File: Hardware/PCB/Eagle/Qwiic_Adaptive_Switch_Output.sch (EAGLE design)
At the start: 60 parts, among them J1 QWIIC_RIGHT_ANGLE, J3 QWIIC_RIGHT_ANGLE, K1 G3VM-41DY1, K2 G3VM-41DY1, SW1 CUI_SJ1-3513, SW2 CUI_SJ1-3513, U1 TCA9534

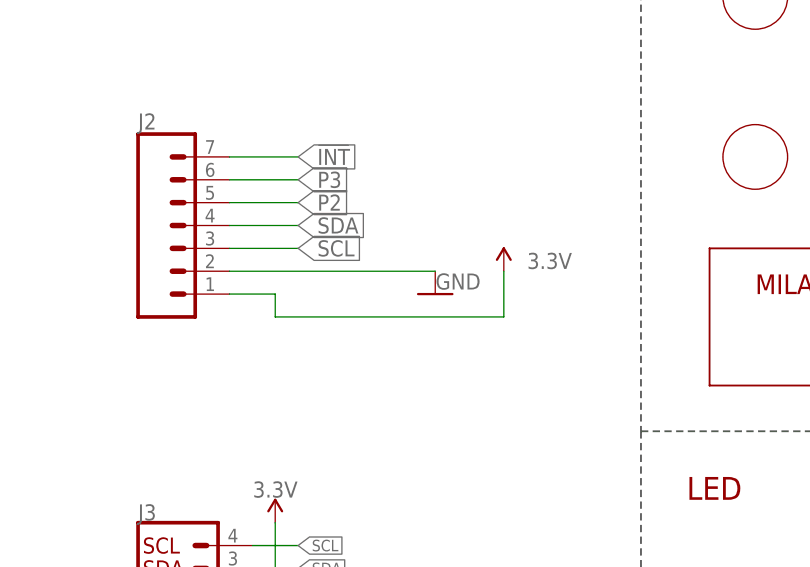
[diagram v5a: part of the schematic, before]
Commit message: Updated header pin order
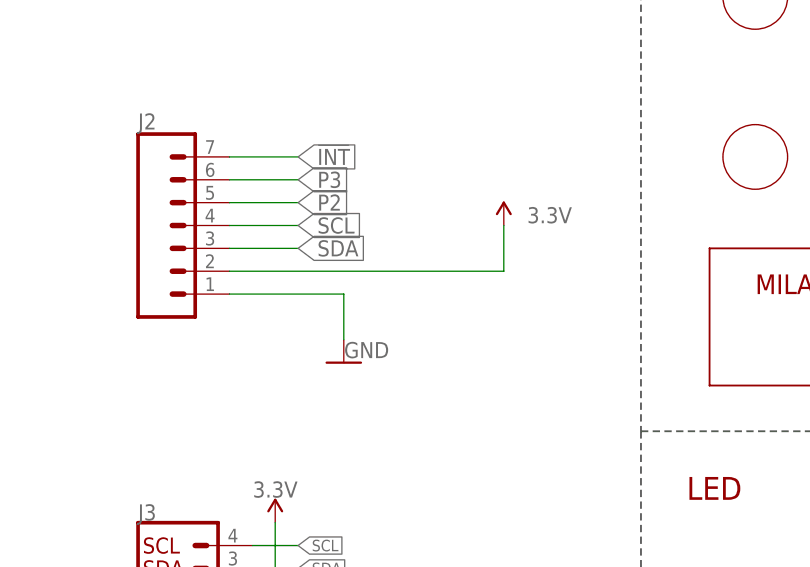
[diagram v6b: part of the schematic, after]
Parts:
- removed JP3: STAND-OFF-3.3, milador:STAND-OFF-3.3
- added H3: STAND-OFF-3.3, milador:STAND-OFF-3.3
- renumbered JP4 to H4
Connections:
- net 3.3V: now also J2.2; no longer J2.1
- net GND: now also J2.1; no longer J2.2
- net SCL: now also J2.4; no longer J2.3
- net SDA: now also J2.3; no longer J2.4
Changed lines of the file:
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@@
 </classes>
 <parts>
-<part name="JP3" library="milador" library_urn="urn:adsk.eagle:library:12595918" deviceset="STAND-OFF-" device="3.3" package3d_urn="urn:adsk.eagle:package:30775189/1"/>
-<part name="JP4" library="milador" library_urn="urn:adsk.eagle:library:12595918" deviceset="STAND-OFF-" device="3.3" package3d_urn="urn:adsk.eagle:package:30775189/1"/>
+<part name="H1" library="milador" library_urn="urn:adsk.eagle:library:12595918" deviceset="STAND-OFF-" device="3.3" package3d_urn="urn:adsk.eagle:package:30775189/1"/>
+<part name="H4" library="milador" library_urn="urn:adsk.eagle:library:12595918" deviceset="STAND-OFF-" device="3.3" package3d_urn="urn:adsk.eagle:package:30775189/1"/>
 <part name="SUPPLY4" library="SparkFun-PowerSymbols" deviceset="3.3V" device=""/>
 <part name="SUPPLY5" library="SparkFun-PowerSymbols" deviceset="3.3V" device=""/>
@@
 <part name="SUPPLY9" library="SparkFun-PowerSymbols" deviceset="3.3V" device=""/>
 <part name="I2C" library="milador_SMD" library_urn="urn:adsk.eagle:library:27847482" deviceset="JUMPERS_JUMPER-SMT_3_2-NC_TRACE" device="_SILK" package3d_urn="urn:adsk.eagle:package:29222217/1"/>
-<part name="H1" library="milador" library_urn="urn:adsk.eagle:library:12595918" deviceset="STAND-OFF-" device="3.3" package3d_urn="urn:adsk.eagle:package:30775189/1"/>
+<part name="H3" library="milador" library_urn="urn:adsk.eagle:library:12595918" deviceset="STAND-OFF-" device="3.3" package3d_urn="urn:adsk.eagle:package:30775189/1"/>
 <part name="H2" library="milador" library_urn="urn:adsk.eagle:library:12595918" deviceset="STAND-OFF-" device="3.3" package3d_urn="urn:adsk.eagle:package:30775189/1"/>
 <part name="R9" library="milador_SMD" library_urn="urn:adsk.eagle:library:27847482" deviceset="RESISTOR-" device="0805-MP" package3d_urn="urn:adsk.eagle:package:27847629/3" value="10k"/>
@@
 </plain>
 <instances>
-<instance part="JP3" gate="G$1" x="243.84" y="223.52" smashed="yes"/>
-<instance part="JP4" gate="G$1" x="243.84" y="210.82" smashed="yes"/>
+<instance part="H1" gate="G$1" x="243.84" y="223.52" smashed="yes"/>
+<instance part="H4" gate="G$1" x="243.84" y="210.82" smashed="yes"/>
 <instance part="SUPPLY4" gate="G$1" x="88.9" y="220.98" smashed="yes" rot="MR0">
 <attribute name="VALUE" x="88.9" y="223.774" size="1.778" layer="96" font="vector" rot="MR0" align="bottom-center"/>
@@
 <attribute name="NAME" x="208.28" y="114.681" size="1.778" layer="95" font="vector" rot="MR0"/>
 </instance>
-<instance part="H1" gate="G$1" x="228.6" y="223.52" smashed="yes"/>
+<instance part="H3" gate="G$1" x="228.6" y="223.52" smashed="yes"/>
 <instance part="H2" gate="G$1" x="228.6" y="210.82" smashed="yes"/>
 <instance part="R9" gate="G$1" x="231.14" y="109.22" smashed="yes" rot="R90">
@@
 <attribute name="NAME" x="73.66" y="183.388" size="1.778" layer="95" font="vector"/>
 </instance>
-<instance part="SUPPLY7" gate="G$1" x="114.3" y="167.64" smashed="yes" rot="MR0">
-<attribute name="VALUE" x="119.38" y="167.894" size="1.778" layer="96" font="vector" rot="MR0" align="bottom-center"/>
-</instance>
-<instance part="GND5" gate="1" x="106.68" y="165.1" smashed="yes">
-<attribute name="VALUE" x="109.22" y="167.386" size="1.778" layer="96" font="vector" align="top-center"/>
+<instance part="SUPPLY7" gate="G$1" x="114.3" y="172.72" smashed="yes" rot="MR0">
+<attribute name="VALUE" x="119.38" y="172.974" size="1.778" layer="96" font="vector" rot="MR0" align="bottom-center"/>
+</instance>
+<instance part="GND5" gate="1" x="96.52" y="157.48" smashed="yes">
+<attribute name="VALUE" x="99.06" y="159.766" size="1.778" layer="96" font="vector" align="top-center"/>
 </instance>
 <instance part="LABEL_3V_TOP" gate="G$1" x="142.24" y="198.12" smashed="yes"/>
@@
 </segment>
 <segment>
+<pinref part="J2" gate="G$1" pin="2"/>
+<wire x1="83.82" y1="167.64" x2="114.3" y2="167.64" width="0.1524" layer="91"/>
 <pinref part="SUPPLY7" gate="G$1" pin="3.3V"/>
-<wire x1="114.3" y1="167.64" x2="114.3" y2="162.56" width="0.1524" layer="91"/>
-<wire x1="114.3" y1="162.56" x2="88.9" y2="162.56" width="0.1524" layer="91"/>
-<wire x1="88.9" y1="162.56" x2="88.9" y2="165.1" width="0.1524" layer="91"/>
-<pinref part="J2" gate="G$1" pin="1"/>
-<wire x1="88.9" y1="165.1" x2="83.82" y2="165.1" width="0.1524" layer="91"/>
+<wire x1="114.3" y1="167.64" x2="114.3" y2="172.72" width="0.1524" layer="91"/>
 </segment>
 </net>
@@
 </segment>
 <segment>
-<pinref part="J2" gate="G$1" pin="2"/>
+<pinref part="J2" gate="G$1" pin="1"/>
 <pinref part="GND5" gate="1" pin="GND"/>
-<wire x1="83.82" y1="167.64" x2="106.68" y2="167.64" width="0.1524" layer="91"/>
+<wire x1="83.82" y1="165.1" x2="96.52" y2="165.1" width="0.1524" layer="91"/>
+<wire x1="96.52" y1="165.1" x2="96.52" y2="160.02" width="0.1524" layer="91"/>
 </segment>
 </net>
@@
 </segment>
 <segment>
-<pinref part="J2" gate="G$1" pin="4"/>
-<wire x1="83.82" y1="172.72" x2="91.44" y2="172.72" width="0.1524" layer="91"/>
-<label x="91.44" y="172.72" size="1.778" layer="95" xref="yes"/>
+<pinref part="J2" gate="G$1" pin="3"/>
+<wire x1="83.82" y1="170.18" x2="91.44" y2="170.18" width="0.1524" layer="91"/>
+<label x="91.44" y="170.18" size="1.778" layer="95" xref="yes"/>
 </segment>
 </net>
@@
 </segment>
 <segment>
-<pinref part="J2" gate="G$1" pin="3"/>
-<wire x1="83.82" y1="170.18" x2="91.44" y2="170.18" width="0.1524" layer="91"/>
-<label x="91.44" y="170.18" size="1.778" layer="95" xref="yes"/>
-</segment>
-</net>
+<pinref part="J2" gate="G$1" pin="4"/>
+<wire x1="83.82" y1="172.72" x2="91.44" y2="172.72" width="0.1524" layer="91"/>
+<label x="91.44" y="172.72" size="1.778" layer="95" xref="yes"/>
+</segment>
+</net>
